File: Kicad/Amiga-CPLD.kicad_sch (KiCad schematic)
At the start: 22 parts, among them CN1 CDTV-DIAG, J1 JTAG, J2 LED, SW1 SW_DIP_x04, U1 AZ1117-3.3, U2 XC95144XL-TQ100, X1 50MHz

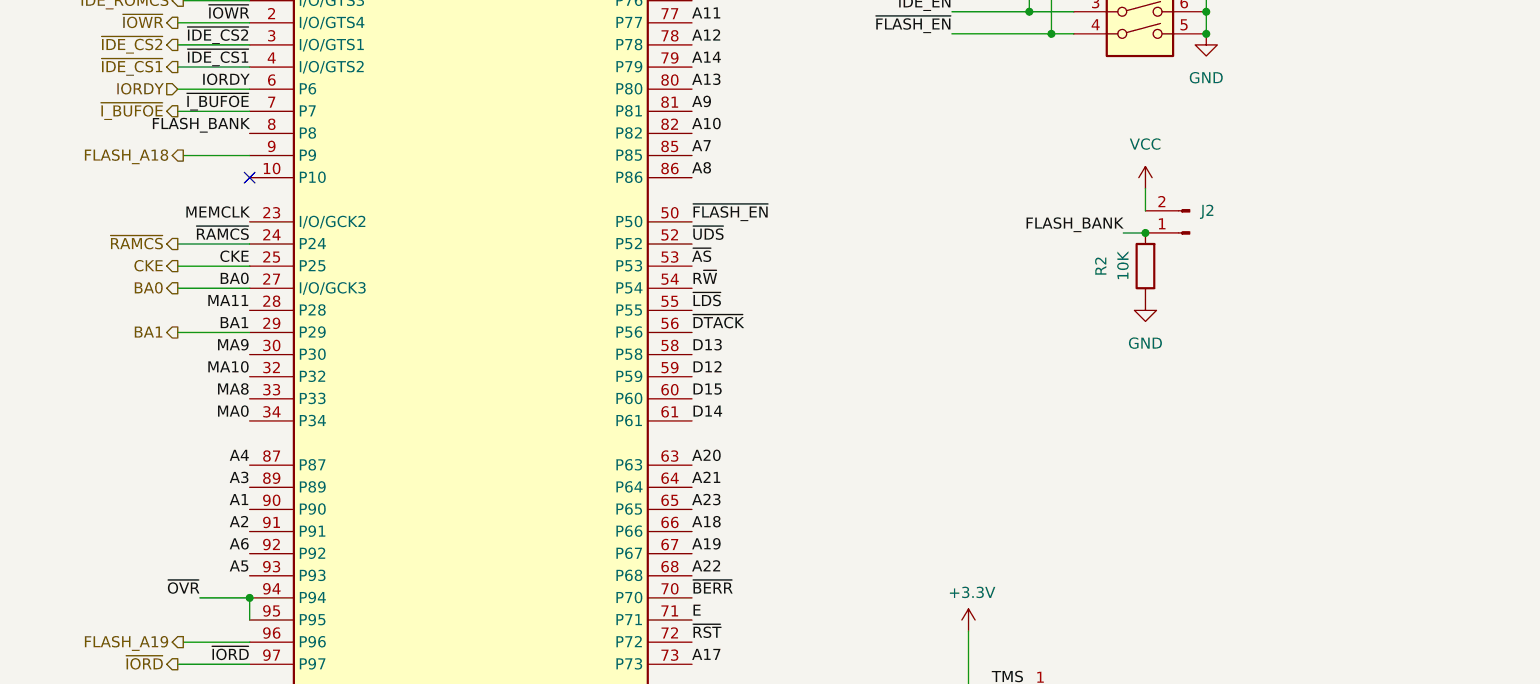
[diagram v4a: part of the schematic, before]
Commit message: Proto B
Add connection to CDTV JP15 to disable extended rom decode when Flash ROM active
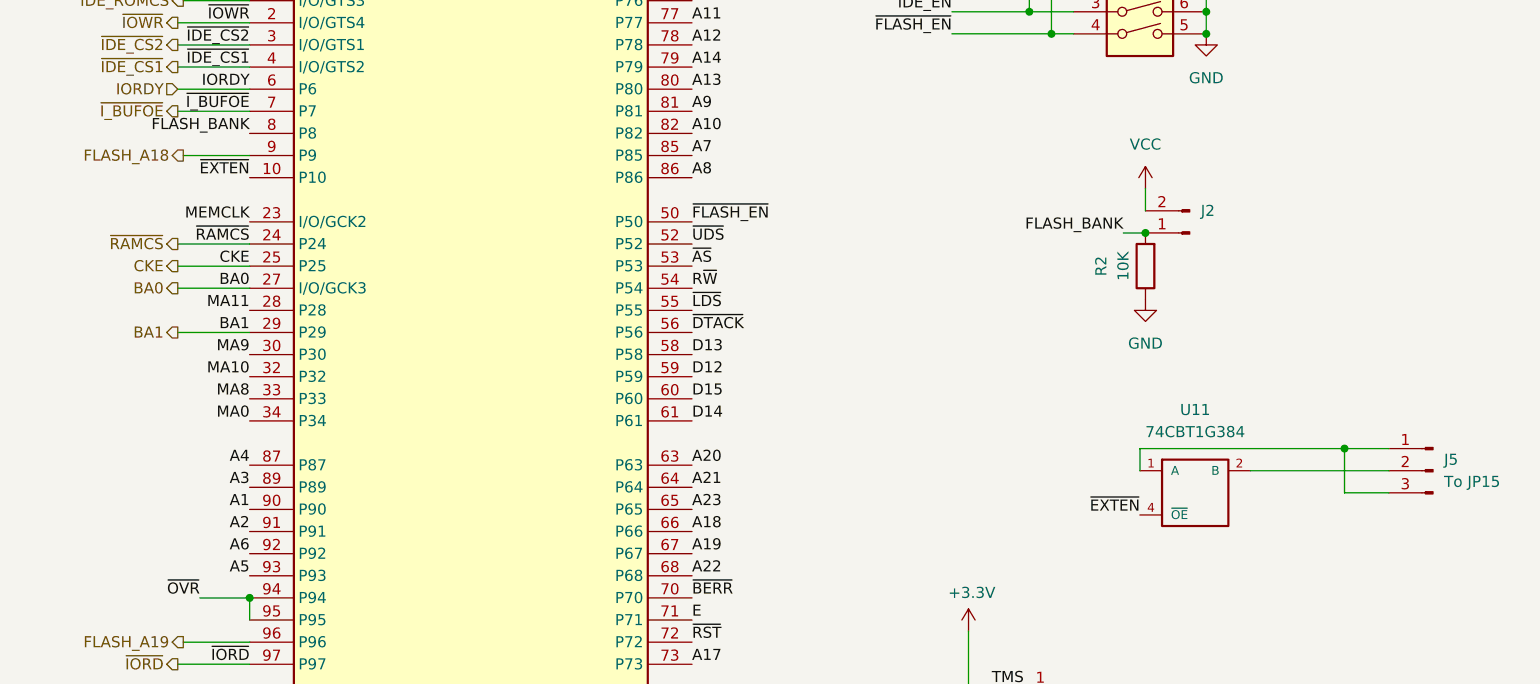
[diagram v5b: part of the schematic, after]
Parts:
- added J5: To JP15, Connector_PinHeader_2.54mm:PinHeader_1x03_P2.54mm_Horizontal, symbol Connector:Conn_01x03_Male
- added U11: 74CBT1G384, Package_TO_SOT_SMD:SOT-23-5, symbol 74xGxx:74CBT1G384
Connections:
- net GND: now also U11.3 (GND)
- net VCC: now also U11.5 (VCC)
- net ~{EXTEN}: now reaches U2.10 (P10)
- net ~{EXTEN}: now also U11.4 (~{OE})
- new net: J5.1 (Pin_1), J5.3 (Pin_3), U11.1 (A)
- new net: J5.2 (Pin_2), U11.2 (B)
- no-connect marks 26 -> 25
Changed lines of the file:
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@@
   (junction (at 161.29 24.13) (diameter 1.016) (color 0 0 0 0)
+  )
+  (junction (at 259.08 116.205) (diameter 0) (color 0 0 0 0)
   )
   (junction (at 163.83 24.13) (diameter 1.016) (color 0 0 0 0)
@@
   (no_connect (at 133.35 39.37))
   (no_connect (at 133.35 41.91))
-  (no_connect (at 133.35 85.09))
   (no_connect (at 40.005 97.79))
   (no_connect (at 40.005 102.87))
@@
     (stroke (width 0) (type default) (color 0 0 0 0))
   )
+  (wire (pts (xy 235.585 116.205) (xy 235.585 118.745))
+    (stroke (width 0) (type default) (color 0 0 0 0))
+  )
   (wire (pts (xy 125.095 95.25) (xy 133.35 95.25))
     (stroke (width 0) (type default) (color 0 0 0 0))
@@
     (stroke (width 0) (type solid) (color 0 0 0 0))
   )
+  (wire (pts (xy 235.585 116.205) (xy 259.08 116.205))
+    (stroke (width 0) (type default) (color 0 0 0 0))
+  )
   (wire (pts (xy 133.35 62.23) (xy 125.73 62.23))
     (stroke (width 0) (type default) (color 0 0 0 0))
@@
     (stroke (width 0) (type default) (color 0 0 0 0))
   )
+  (wire (pts (xy 248.285 118.745) (xy 264.16 118.745))
+    (stroke (width 0) (type default) (color 0 0 0 0))
+  )
   (wire (pts (xy 81.915 44.45) (xy 86.995 44.45))
     (stroke (width 0) (type default) (color 0 0 0 0))
@@
     (stroke (width 0) (type default) (color 0 0 0 0))
   )
+  (wire (pts (xy 259.08 116.205) (xy 264.16 116.205))
+    (stroke (width 0) (type default) (color 0 0 0 0))
+  )
   (wire (pts (xy 151.13 161.29) (xy 153.67 161.29))
     (stroke (width 0) (type solid) (color 0 0 0 0))
@@
     (stroke (width 0) (type default) (color 0 0 0 0))
   )
+  (wire (pts (xy 264.16 121.285) (xy 259.08 121.285))
+    (stroke (width 0) (type default) (color 0 0 0 0))
+  )
   (wire (pts (xy 127.635 133.35) (xy 133.35 133.35))
     (stroke (width 0) (type default) (color 0 0 0 0))
@@
     (stroke (width 0) (type default) (color 0 0 0 0))
   )
+  (wire (pts (xy 259.08 121.285) (xy 259.08 116.205))
+    (stroke (width 0) (type default) (color 0 0 0 0))
+  )
   (wire (pts (xy 34.29 120.65) (xy 34.29 123.19))
     (stroke (width 0) (type default) (color 0 0 0 0))
@@
     (effects (font (size 1.27 1.27)) (justify left bottom))
   )
+  (label "~{EXTEN}" (at 235.585 123.825 180)
+    (effects (font (size 1.27 1.27)) (justify right bottom))
+  )
   (label "~{R_BUFOE}" (at 133.35 44.45 180)
     (effects (font (size 1.27 1.27)) (justify right bottom))
@@
   (label "A14" (at 184.15 72.39 0)
     (effects (font (size 1.27 1.27)) (justify left bottom))
+  )
+  (label "~{EXTEN}" (at 133.35 85.09 180)
+    (effects (font (size 1.27 1.27)) (justify right bottom))
   )
   (label "MA5" (at 184.15 41.91 0)
@@
     (pin "99")
   )
+  (symbol (lib_id "74xGxx:74CBT1G384") (at 241.935 121.285 0) (unit 1)
+    (in_bom yes) (on_board yes) (fields_autoplaced)
+    (property "Reference" "U11" (id 0) (at 241.935 111.76 0))
+    (property "Value" "74CBT1G384" (id 1) (at 241.935 114.3 0))
+    (property "Footprint" "Package_TO_SOT_SMD:SOT-23-5" (id 2) (at 241.935 121.285 0)
+      (effects (font (size 1.27 1.27)) hide)
+    )
+    (property "Datasheet" "http://www.ti.com/lit/sg/scyt129e/scyt129e.pdf" (id 3) (at 241.935 121.285 0)
+      (effects (font (size 1.27 1.27)) hide)
+    )
+    (pin "1")
+    (pin "2")
+    (pin "3")
+    (pin "4")
+    (pin "5")
+  )
   (symbol (lib_id "Device:R_Pack04") (at 220.345 52.07 0) (mirror y) (unit 1)
     (in_bom yes) (on_board yes)
@@
     (pin "2")
   )
+  (symbol (lib_id "Connector:Conn_01x03_Male") (at 269.24 118.745 0) (mirror y) (unit 1)
+    (in_bom yes) (on_board yes) (fields_autoplaced)
+    (property "Reference" "J5" (id 0) (at 270.51 117.4749 0)
+      (effects (font (size 1.27 1.27)) (justify right))
+    )
+    (property "Value" "To JP15" (id 1) (at 270.51 120.0149 0)
+      (effects (font (size 1.27 1.27)) (justify right))
+    )
+    (property "Footprint" "Connector_PinHeader_2.54mm:PinHeader_1x03_P2.54mm_Horizontal" (id 2) (at 269.24 118.745 0)
+      (effects (font (size 1.27 1.27)) hide)
+    )
+    (property "Datasheet" "~" (id 3) (at 269.24 118.745 0)
+      (effects (font (size 1.27 1.27)) hide)
+    )
+    (pin "1")
+    (pin "2")
+    (pin "3")
+  )
   (symbol (lib_id "power:GND") (at 93.98 165.735 0) (unit 1)

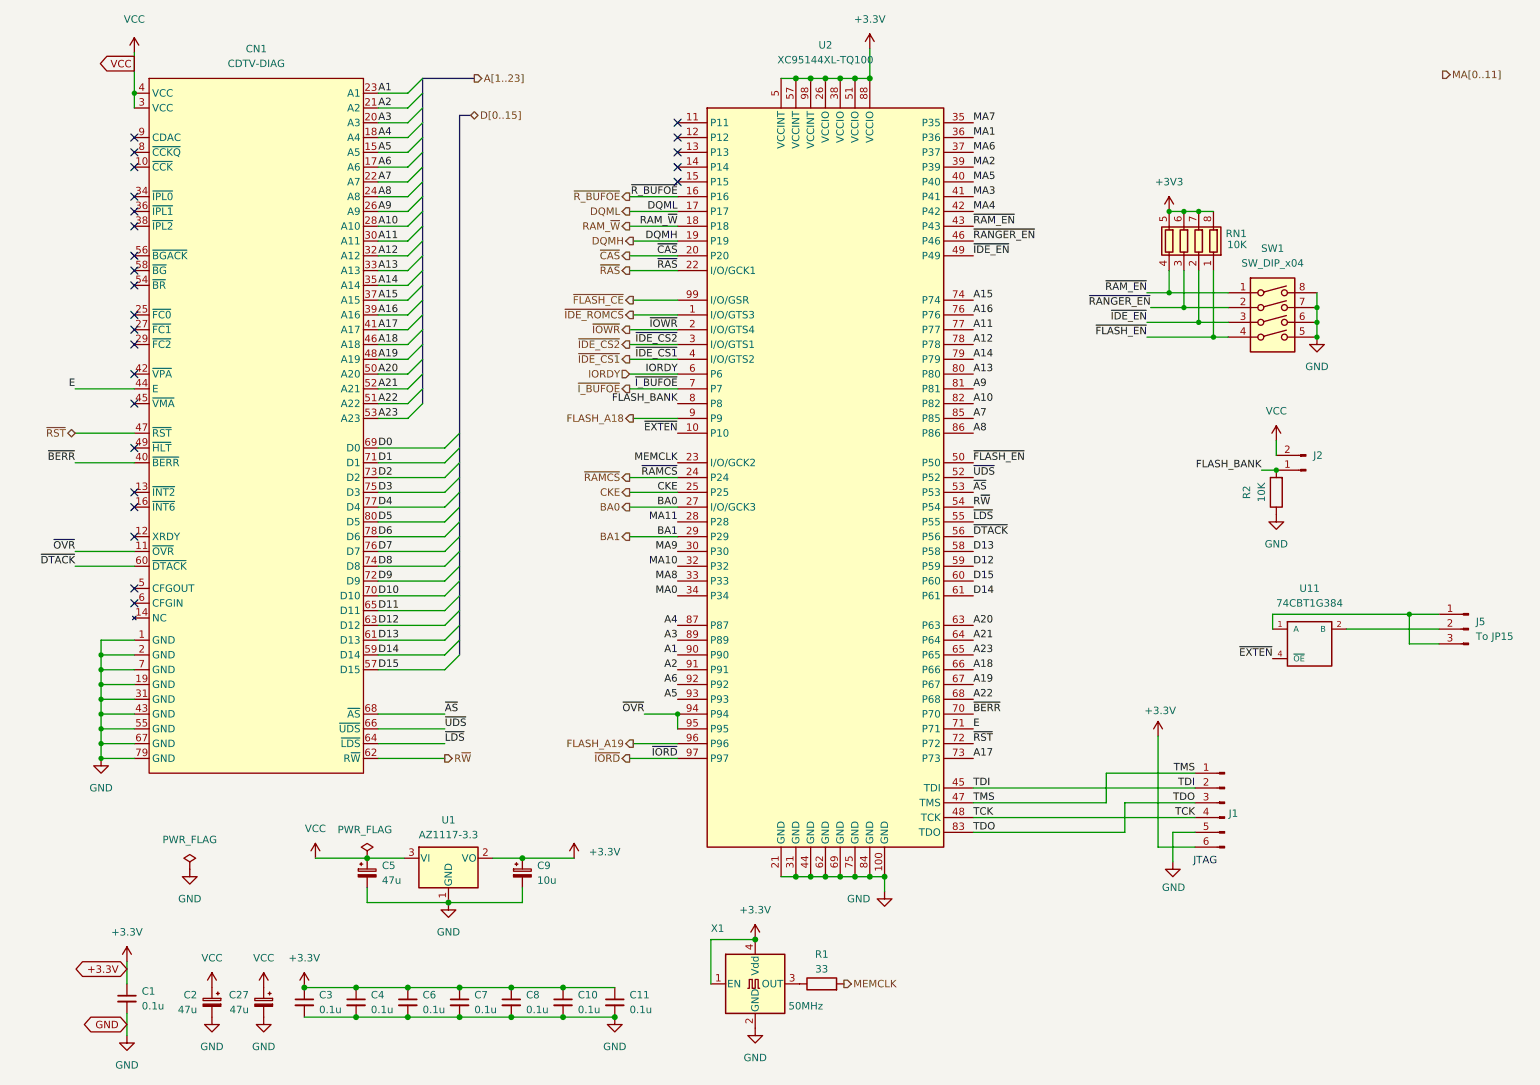
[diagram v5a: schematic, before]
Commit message: Proto_B: Add A500 mode jumper, add SMD Act LED
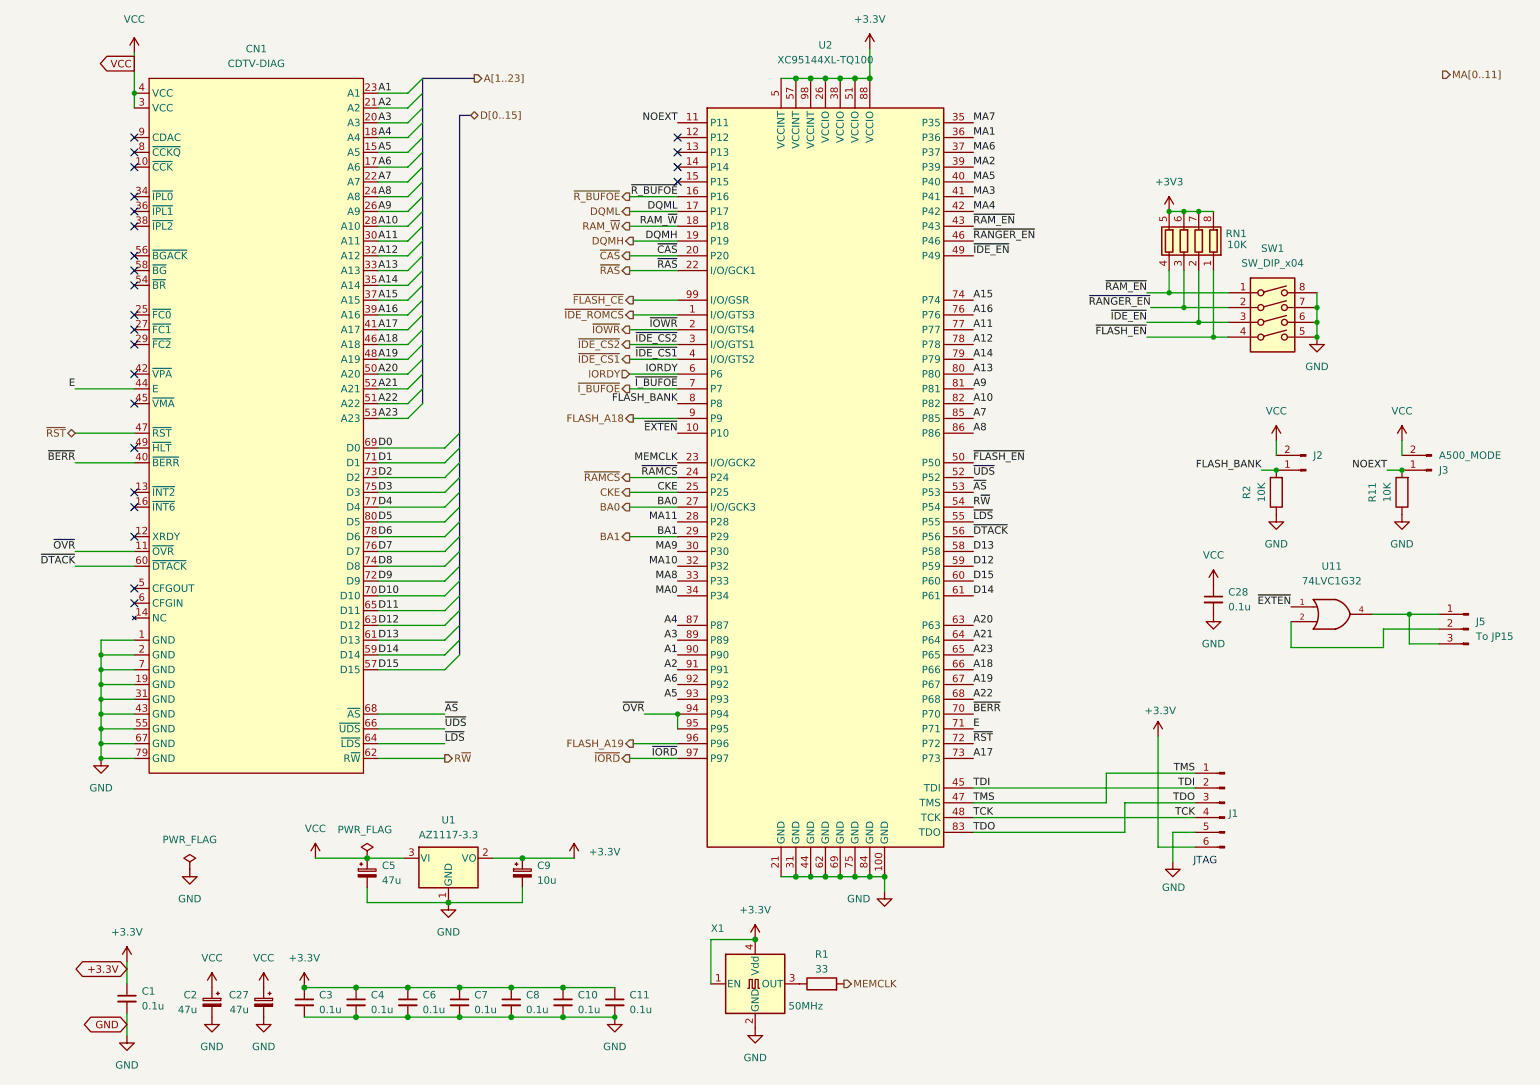
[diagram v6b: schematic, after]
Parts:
- removed U11: 74CBT1G384, Package_TO_SOT_SMD:SOT-23-5, symbol 74xGxx:74CBT1G384
- added C28: 0.1u, Capacitor_SMD:C_0603_1608Metric, symbol Device:C_Small
- added J3: A500_MODE, Connector_PinHeader_2.00mm:PinHeader_1x02_P2.00mm_Vertical, symbol Connector:Conn_01x02_Male
- added R11: 10K, Resistor_SMD:R_0603_1608Metric, symbol Device:R
- added U11: 74LVC1G32, Package_TO_SOT_SMD:SOT-23-5, symbol 74xGxx:74LVC1G32
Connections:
- net GND: now also C28.2, R11.1, U11.3 (GND)
- net VCC: now also C28.1, J3.2 (Pin_2), U11.5 (VCC)
- net ~{EXTEN}: now also U11.1
- net NOEXT: now reaches U2.11 (P11)
- net NOEXT: now also J3.1 (Pin_1), R11.2
- net at J5.1 (Pin_1), J5.3 (Pin_3): now also U11.4
- net at J5.2 (Pin_2): now also U11.2
- no-connect marks 25 -> 24

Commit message: Fixup some of the JLC part numbers
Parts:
- U1: LCSC # C460428 -> C362111
- U11: LCSC # C12516 -> C10096
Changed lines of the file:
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@@
       (effects (font (size 1.27 1.27)) hide)
     )
-    (property "LCSC #" "C460428" (id 4) (at 93.98 158.115 0)
+    (property "LCSC #" " C362111" (id 4) (at 93.98 158.115 0)
       (effects (font (size 1.27 1.27)) hide)
     )
@@
       (effects (font (size 1.27 1.27)) hide)
     )
-    (property "LCSC #" "C12516" (id 4) (at 246.38 116.205 0)
-      (effects (font (size 1.27 1.27)) hide)
-    )
+    (property "LCSC #" "C10096" (id 4) (at 246.38 116.205 0)
+      (effects (font (size 1.27 1.27)) hide)
+    )

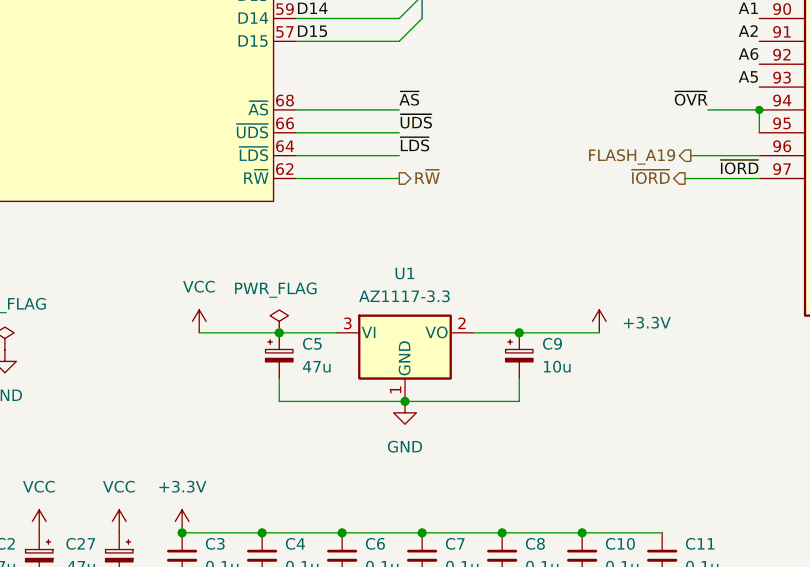
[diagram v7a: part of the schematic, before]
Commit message: Rev_A: Fixup JLC Part # for Volt reg
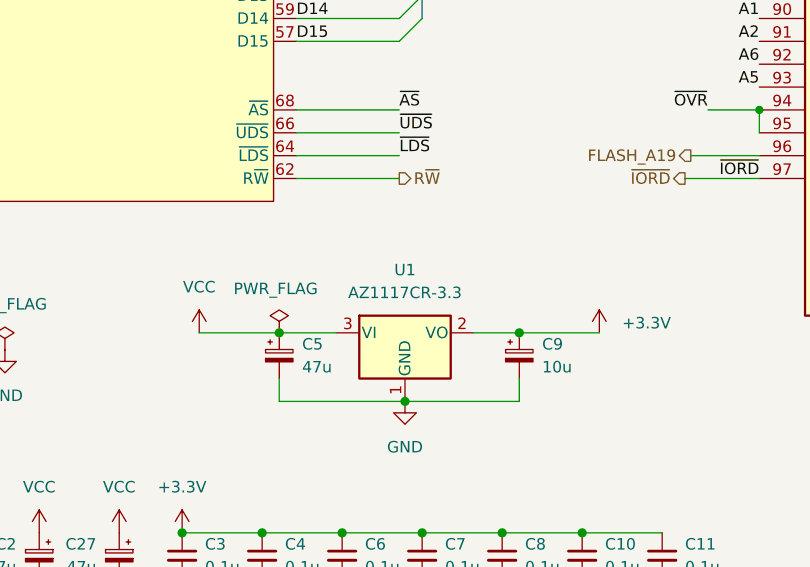
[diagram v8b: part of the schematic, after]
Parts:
- U1: value AZ1117-3.3 -> AZ1117CR-3.3; LCSC # C362111 -> C460428
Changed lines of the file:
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@@
   (symbol (lib_id "Regulator_Linear:AZ1117-3.3") (at 93.98 158.115 0) (unit 1)
     (in_bom yes) (on_board yes) (fields_autoplaced)
-    (property "Reference" "U1" (id 0) (at 93.98 151.5618 0))
-    (property "Value" "AZ1117-3.3" (id 1) (at 93.98 154.1018 0))
+    (property "Reference" "U1" (id 0) (at 93.98 151.13 0))
+    (property "Value" "AZ1117CR-3.3" (id 1) (at 93.98 153.67 0))
     (property "Footprint" "Package_TO_SOT_SMD:SOT-89-3" (id 2) (at 93.98 151.765 0)
       (effects (font (size 1.27 1.27) italic) hide)
@@
       (effects (font (size 1.27 1.27)) hide)
     )
-    (property "LCSC #" " C362111" (id 4) (at 93.98 158.115 0)
+    (property "LCSC #" "C460428" (id 4) (at 93.98 158.115 0)
       (effects (font (size 1.27 1.27)) hide)
     )
